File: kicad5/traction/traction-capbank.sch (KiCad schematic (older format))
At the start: 26 parts

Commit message: Rev A.4.3: fourth review round — LCOR reconciled, UB15 compensation (F58-F59)
- F58: LCOR netlist value became 2.2uH in A.4.2 but the parts-db class
  MPN kept printing IND-4.7uH-2A on the sheet and BOM - an assembler
  would fit the old part. MPN/desc now carry 2.2uH + the OTP pairing;
  value, sheet, BOM and CORE_LSEL_OTP=0x02 agree end-to-end.
- F59: TPS55340 COMP had only 10nF to ground (no zero; ~0deg screening
  phase margin in the CCM model). Series R3/C4 = 2k/100nF per TI
  8.2.1.2.11 + 470pF HF pole cap; RHPZ ~450kHz not limiting; measured
  Bode stays a bench gate.
- Narrative corrections per review: CBOOT_PRE 100nF was legal (Rev 6.1
  allows 22-100nF; 22nF kept as typ) - F52 log softened; VCC1 loss
  reclassified as a single initiating failure (UGDL open output) whose
  outcome is three-phase-open with ASC still commandable.

Gates: 1695/1695 pins, ERC 782/0, design-verify 75P/3W/0F,
BOM Rs.70,091 @1k, 592 components, 193 lines.

Co-Authored-By: Claude Fable 5 <noreply@anthropic.com>
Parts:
- removed JCBDN, JCBDP: STUD-M6, StudM6, symbol traction-r1:TERM_1
- added CDC8, CDC9: 20uF, FilmCan37.5, symbol traction-r1:C
- JCBDN: renamed from JCBEN; value STUD-M8 -> STUD-M6; footprint StudM8 -> StudM6; MPN STUD-M8 -> STUD-M6
- JCBDP: renamed from JCBEP; value STUD-M8 -> STUD-M6; footprint StudM8 -> StudM6; MPN STUD-M8 -> STUD-M6
- JCBEN: renamed from JCBUN; value TAB-M6 -> STUD-M8; footprint TabM6 -> StudM8; MPN TAB-M6 -> STUD-M8
- JCBEP: renamed from JCBUP; value TAB-M6 -> STUD-M8; footprint TabM6 -> StudM8; MPN TAB-M6 -> STUD-M8
- JCBWN: renamed from CDC1; value 20uF -> TAB-M6; footprint FilmCan37.5 -> TabM6; symbol traction-r1:C -> traction-r1:TERM_1; LCSC C2840809 -> CLASS; MPN C3D1M206KFSA382 -> TAB-M6
- JCBWP: renamed from CDC10; value 20uF -> TAB-M6; footprint FilmCan37.5 -> TabM6; symbol traction-r1:C -> traction-r1:TERM_1; LCSC C2840809 -> CLASS; MPN C3D1M206KFSA382 -> TAB-M6
- renumbered CDC11 to CDC1, CDC12 to CDC10, CDC13 to CDC11, CDC14 to CDC12, CDC15 to CDC13, CDC16 to CDC14, CDC2 to CDC15, CDC3 to CDC16, CDC4 to CDC2, CDC5 to CDC3, CDC6 to CDC4, CDC7 to CDC5, CDC8 to CDC6, CDC9 to CDC7, JCBVN to JCBUN, JCBVP to JCBUP, JCBWN to JCBVN, JCBWP to JCBVP
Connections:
- net DCN: now also JCBWN.1 (P), CDC8.2, CDC9.2; no longer JCBWN.2, JCBWP.2
- net DCP: now also CDC8.1, CDC9.1; no longer JCBWN.1
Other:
- note added: "220 kW pk Cap bank (HV, busbar) - 2 of 4 · rev A.4.3 · 2 sections · 26 components"
- note removed: "220 kW pk Cap bank (HV, busbar) - 2 of 4 · rev A.4.2 · 2 sections · 26 components"
- moved on the sheet: CDC1, CDC10, CDC11, CDC12, CDC13, CDC14, CDC15, CDC16, CDC2, CDC3, CDC4, CDC5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
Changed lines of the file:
@@
 Title "Traction Inverter — Cap bank (busbar assembly, 320 uF)"
 Date "2026-09-09"
-Rev "A.4.2"
+Rev "A.4.3"
 Comp "Traction Inverter 220 kW pk - Cap bank (HV, busbar), sheet 2 of 4"
 Comment1 "Inverter = Power board + Cap bank busbar + bolt-on Discharge board (all HV) + Control card (LV); safe state holds with any link lost"
@@
 $EndDescr
 Text Notes 600 5100 0    60   ~ 12
-220 kW pk Cap bank (HV, busbar) - 2 of 4   ·   rev A.4.2   ·   2 sections   ·   26 components
+220 kW pk Cap bank (HV, busbar) - 2 of 4   ·   rev A.4.3   ·   2 sections   ·   26 components
 Text Notes 600 5400 0    50   ~ 0
 NET NAMING: U<ref>_<PIN> = node at that IC pin   ·   R<stem>_M = series-pair midpoint   ·   R<stem>_<nm> = tap between R<stem>n/m   ·   all others are explicit design nets   ·   same name on another sheet = same net, joined only at the named connector/stud/tab
@@
 $Comp
 L traction-r1:TERM_1 JCBDN
-U 1 1 5E000123
+U 1 1 5E000125
 P 1250 2350
 F 0 "JCBDN" H 1250 2190 50  0000 C CNN
@@
 $Comp
 L traction-r1:TERM_1 JCBDP
-U 1 1 5E000124
+U 1 1 5E000126
 P 1250 1950
 F 0 "JCBDP" H 1250 1790 50  0000 C CNN
@@
 $Comp
 L traction-r1:TERM_1 JCBEN
-U 1 1 5E000125
+U 1 1 5E000127
 P 1250 1550
 F 0 "JCBEN" H 1250 1390 50  0000 C CNN
@@
 $Comp
 L traction-r1:TERM_1 JCBEP
-U 1 1 5E000126
+U 1 1 5E000128
 P 1250 1150
 F 0 "JCBEP" H 1250 990 50  0000 C CNN
@@
 $Comp
 L traction-r1:TERM_1 JCBUN
-U 1 1 5E000127
+U 1 1 5E000129
 P 2150 1550
 F 0 "JCBUN" H 2150 1390 50  0000 C CNN
@@
 $Comp
 L traction-r1:TERM_1 JCBUP
-U 1 1 5E000128
+U 1 1 5E00012A
 P 2150 1150
 F 0 "JCBUP" H 2150 990 50  0000 C CNN
@@
 $Comp
 L traction-r1:TERM_1 JCBVN
-U 1 1 5E000129
+U 1 1 5E00012B
 P 2150 2350
 F 0 "JCBVN" H 2150 2190 50  0000 C CNN
@@
 $Comp
 L traction-r1:TERM_1 JCBVP
-U 1 1 5E00012A
+U 1 1 5E00012C
 P 2150 1950
 F 0 "JCBVP" H 2150 1790 50  0000 C CNN
@@
 $Comp
 L traction-r1:TERM_1 JCBWN
-U 1 1 5E00012B
+U 1 1 5E00012D
 P 2150 3150
 F 0 "JCBWN" H 2150 2990 50  0000 C CNN
@@
 $Comp
 L traction-r1:TERM_1 JCBWP
-U 1 1 5E00012C
+U 1 1 5E00012E
 P 2150 2750
 F 0 "JCBWP" H 2150 2590 50  0000 C CNN
@@
 $Comp
 L traction-r1:C CDC1
-U 1 1 5E00012D
+U 1 1 5E00012F
 P 4550 1150
 F 0 "CDC1" H 4550 990 50  0000 C CNN
@@
 $Comp
 L traction-r1:C CDC10
-U 1 1 5E00012E
+U 1 1 5E000130
 P 6050 1550
 F 0 "CDC10" H 6050 1390 50  0000 C CNN
@@
 $Comp
 L traction-r1:C CDC11
-U 1 1 5E00012F
+U 1 1 5E000131
 P 6050 1950
 F 0 "CDC11" H 6050 1790 50  0000 C CNN
@@
 $Comp
 L traction-r1:C CDC12
-U 1 1 5E000130
+U 1 1 5E000132
 P 6050 2350
 F 0 "CDC12" H 6050 2190 50  0000 C CNN
@@
 $Comp
 L traction-r1:C CDC13
-U 1 1 5E000131
+U 1 1 5E000133
 P 6050 2750
 F 0 "CDC13" H 6050 2590 50  0000 C CNN
@@
 $Comp
 L traction-r1:C CDC14
-U 1 1 5E000132
+U 1 1 5E000134
 P 6050 3150
 F 0 "CDC14" H 6050 2990 50  0000 C CNN
@@
 $Comp
 L traction-r1:C CDC15
-U 1 1 5E000133
+U 1 1 5E000135
 P 6050 3550
 F 0 "CDC15" H 6050 3390 50  0000 C CNN
@@
 $Comp
 L traction-r1:C CDC16
-U 1 1 5E000134
+U 1 1 5E000136
 P 6050 3950
 F 0 "CDC16" H 6050 3790 50  0000 C CNN
@@
 $Comp
 L traction-r1:C CDC2
-U 1 1 5E000135
+U 1 1 5E000137
 P 4550 1550
 F 0 "CDC2" H 4550 1390 50  0000 C CNN
@@
 $Comp
 L traction-r1:C CDC3
-U 1 1 5E000136
+U 1 1 5E000138
 P 4550 1950
 F 0 "CDC3" H 4550 1790 50  0000 C CNN
@@
 $Comp
 L traction-r1:C CDC4
-U 1 1 5E000137
+U 1 1 5E000139
 P 4550 2350
 F 0 "CDC4" H 4550 2190 50  0000 C CNN
@@
 $Comp
 L traction-r1:C CDC5
-U 1 1 5E000138
+U 1 1 5E00013A
 P 4550 2750
 F 0 "CDC5" H 4550 2590 50  0000 C CNN
@@
 $Comp
 L traction-r1:C CDC6
-U 1 1 5E000139
+U 1 1 5E00013B
 P 4550 3150
 F 0 "CDC6" H 4550 2990 50  0000 C CNN
@@
 $Comp
 L traction-r1:C CDC7
-U 1 1 5E00013A
+U 1 1 5E00013C
 P 4550 3550
 F 0 "CDC7" H 4550 3390 50  0000 C CNN
@@
 $Comp
 L traction-r1:C CDC8
-U 1 1 5E00013B
+U 1 1 5E00013D
 P 4550 3950
 F 0 "CDC8" H 4550 3790 50  0000 C CNN
@@
 $Comp
 L traction-r1:C CDC9
-U 1 1 5E00013C
+U 1 1 5E00013E
 P 6050 1150
 F 0 "CDC9" H 6050 990 50  0000 C CNN

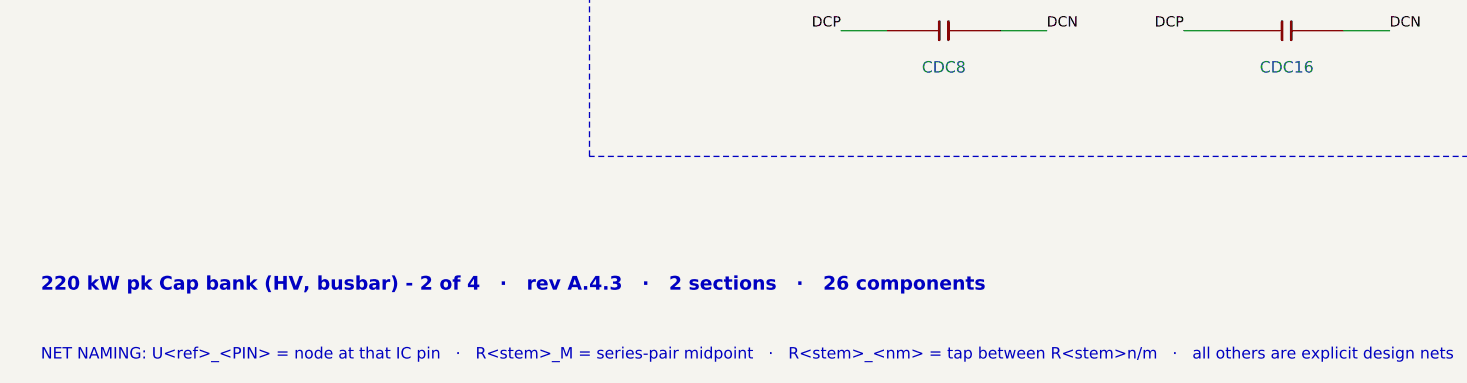
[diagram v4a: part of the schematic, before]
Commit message: Rev A.4.4: round five — bind class MPNs to real parts, pin FS26 OTP config
No electrical change. Procurement closure of the review's remaining
generic identifiers, each verified against its manufacturer datasheet:

- LCOR -> Coilcraft XAL4020-222MEC (2.2uH molded, AEC-Q200; values
  read from the XAL4000 datasheet, now in docs/datasheets)
- LB15 + LSBC -> XAL4040-103MEC (one 10uH line item for both; LSBC
  pairing with FPRE_OTP=450kHz documented per the FS26 DS)
- PS5B/PS5C -> Murata MGJ2D150505SC (+5V output used) behind an
  explicit PO gate: verify reinforced-insulation characterization at
  850VDC working and the SIP-7 pin map before ordering
- RECOM R15P05S evaluated and REJECTED during binding: its 6.4kV is a
  1-second test voltage; IEC 62368-1 insulation grade is BASIC at
  250VACrms working - fails the 850V barrier rule. Rejection recorded
  in design-basis 11e and the BOM row so it cannot be substituted in.
- FS26 OTP configuration pinned as design-basis 8a table (VPRE 6.0V,
  FPRE 450kHz, CORE_LSEL=0x02, VCORE 1.5V, LDO1/2 3.3/5.0V, VMONEXT
  0.8V ref, TRK slots off, VBST disabled, WK2PD/IO2PD set) - the
  ordering step must match it; the family label alone is not evidence.

Gates unchanged: 1695/1695 pins, ERC 782/0, design-verify 75P/3W/0F,
sim-verify 18P/1W/0F. BOM Rs.70,934 @1k with real part prices.

Co-Authored-By: Claude Fable 5 <noreply@anthropic.com>
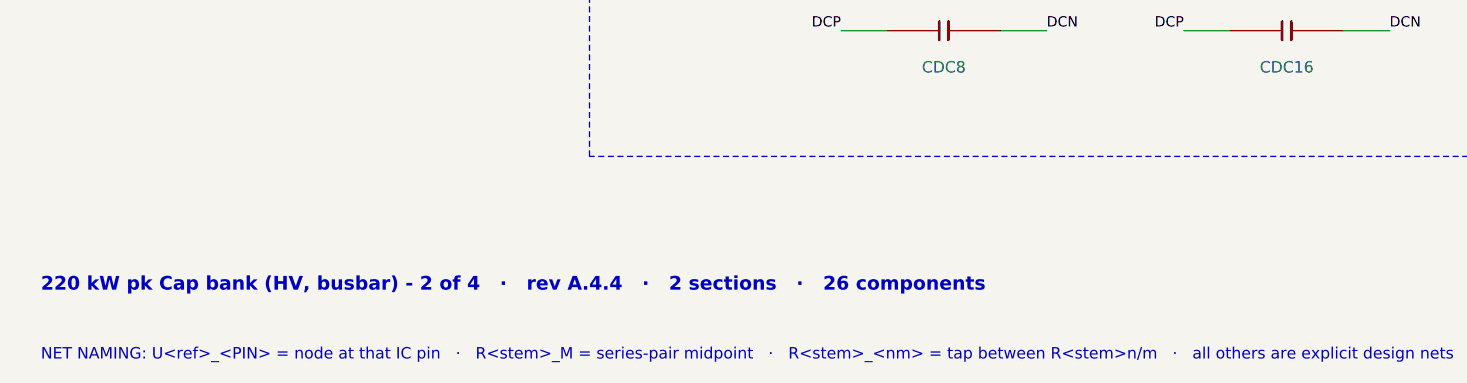
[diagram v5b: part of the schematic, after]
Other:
- note added: "220 kW pk Cap bank (HV, busbar) - 2 of 4 · rev A.4.4 · 2 sections · 26 components"
- note removed: "220 kW pk Cap bank (HV, busbar) - 2 of 4 · rev A.4.3 · 2 sections · 26 components"
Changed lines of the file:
@@
 Title "Traction Inverter — Cap bank (busbar assembly, 320 uF)"
 Date "2026-09-09"
-Rev "A.4.3"
+Rev "A.4.4"
 Comp "Traction Inverter 220 kW pk - Cap bank (HV, busbar), sheet 2 of 4"
 Comment1 "Inverter = Power board + Cap bank busbar + bolt-on Discharge board (all HV) + Control card (LV); safe state holds with any link lost"
@@
 $EndDescr
 Text Notes 600 5100 0    60   ~ 12
-220 kW pk Cap bank (HV, busbar) - 2 of 4   ·   rev A.4.3   ·   2 sections   ·   26 components
+220 kW pk Cap bank (HV, busbar) - 2 of 4   ·   rev A.4.4   ·   2 sections   ·   26 components
 Text Notes 600 5400 0    50   ~ 0
 NET NAMING: U<ref>_<PIN> = node at that IC pin   ·   R<stem>_M = series-pair midpoint   ·   R<stem>_<nm> = tap between R<stem>n/m   ·   all others are explicit design nets   ·   same name on another sheet = same net, joined only at the named connector/stud/tab

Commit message: Rev A.5: end-to-end documentation refresh + 3 defects the audit caught
Docs (every file rewritten to the released state, history kept as
labeled evidence):
- README: five stacked review paragraphs consolidated into one campaign
  table (F1-F62); new Simulation section with the S1-S7 results table
  and all five SVG plots; badges/stats/mermaids/DFM rows refreshed
  (UCC28C40, four-assembly build flow, 770669-1, sim badge, rev A.5)
- design-basis: gate-drive/LV sections describe the released circuit
  (UCC28C40+BUK7Y14+SMAJ13A clamp, boost->ULDO15 chain, MGJ2+QA01C
  bias set, QA01C +20/-4V note)
- dfm.md + cost-rollup.md rewritten (four assemblies, current tiers,
  76% module share, PO gates, banned-substitute rule)
- EXTRACTED-PARAMS: superseded sections replaced (BUK7Y14, winding
  dots, UCC28C40 UVLO), 10 new part sections, fresh 47-PDF archive
  index with evidence files labeled; SMAJ + TE-770669-1 datasheets
  added; wrong-part PDF from a mirror detected and discarded
- calculations/rev.mjs: single REV source imported by every generator
  (the stale-rev defect class is now structurally impossible)

Defects the audit caught and fixed:
- F60: JVEH was bound to TE 776231-1 "AMPSEAL 23" - its own TE drawing
  shows the 35-pos header (mates 776164). Rebound to 770669-1 (true
  23-pos, mates the 770680-1 plug); drawing archived.
- F61: QA01C DS row is +20/-4V (rails named V18*) - clamps verified
  for +20V; QDIS gate 19.5V vs +22 abs WARN row added.
- F62: the on-sheet ASIL-D + DISCHARGE panel had silently vanished
  from the power sheet as it grew through A.4.x. Placement now retries
  every void and extends the sheet if none fits; a power sheet without
  the panel REFUSES to build. Panel text refreshed (full DRV_EN chain,
  57s bleed, "never energize w/o the DISCHARGE BOARD fitted").

Gates: 1695/1695 pins, ERC 782/0, design-verify 75P/4W/0F, sim-verify
18P/1W/0F, BOM Rs.70,934. Power sheet 44.6x28.6 in (panel row added).

Co-Authored-By: Claude Fable 5 <noreply@ant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
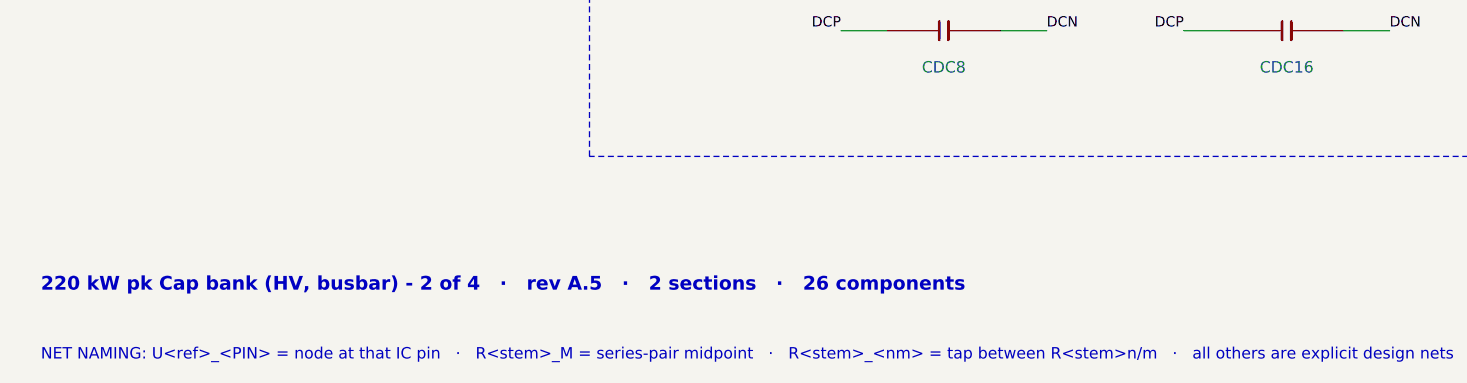
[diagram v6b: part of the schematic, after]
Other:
- note added: "220 kW pk Cap bank (HV, busbar) - 2 of 4 · rev A.5 · 2 sections · 26 components"
- note removed: "220 kW pk Cap bank (HV, busbar) - 2 of 4 · rev A.4.4 · 2 sections · 26 components"
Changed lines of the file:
@@
 Title "Traction Inverter — Cap bank (busbar assembly, 320 uF)"
 Date "2026-09-09"
-Rev "A.4.4"
+Rev "A.5"
 Comp "Traction Inverter 220 kW pk - Cap bank (HV, busbar), sheet 2 of 4"
 Comment1 "Inverter = Power board + Cap bank busbar + bolt-on Discharge board (all HV) + Control card (LV); safe state holds with any link lost"
@@
 $EndDescr
 Text Notes 600 5100 0    60   ~ 12
-220 kW pk Cap bank (HV, busbar) - 2 of 4   ·   rev A.4.4   ·   2 sections   ·   26 components
+220 kW pk Cap bank (HV, busbar) - 2 of 4   ·   rev A.5   ·   2 sections   ·   26 components
 Text Notes 600 5400 0    50   ~ 0
 NET NAMING: U<ref>_<PIN> = node at that IC pin   ·   R<stem>_M = series-pair midpoint   ·   R<stem>_<nm> = tap between R<stem>n/m   ·   all others are explicit design nets   ·   same name on another sheet = same net, joined only at the named connector/stud/tab
